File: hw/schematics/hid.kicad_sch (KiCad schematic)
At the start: 114 parts, among them M1 SK8701-01-004-MODULE, M2 SK8701-01-004-SENSOR, SW1 SW_Push, SW10 SW_Push, SW11 SW_Push, SW12 SW_Push, SW13 SW_Push, SW14 SW_Push, SW15 SW_Push, SW16 SW_Push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

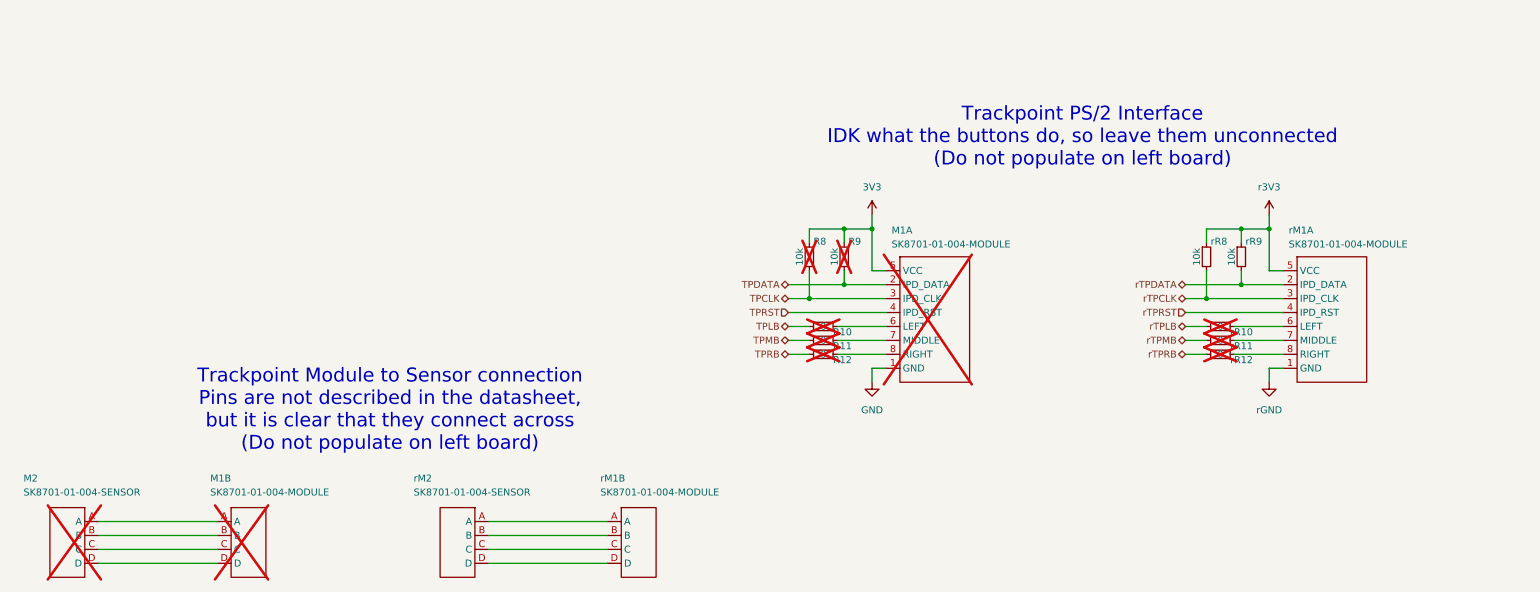
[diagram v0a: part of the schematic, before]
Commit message: Remove FPGA, no longer needed
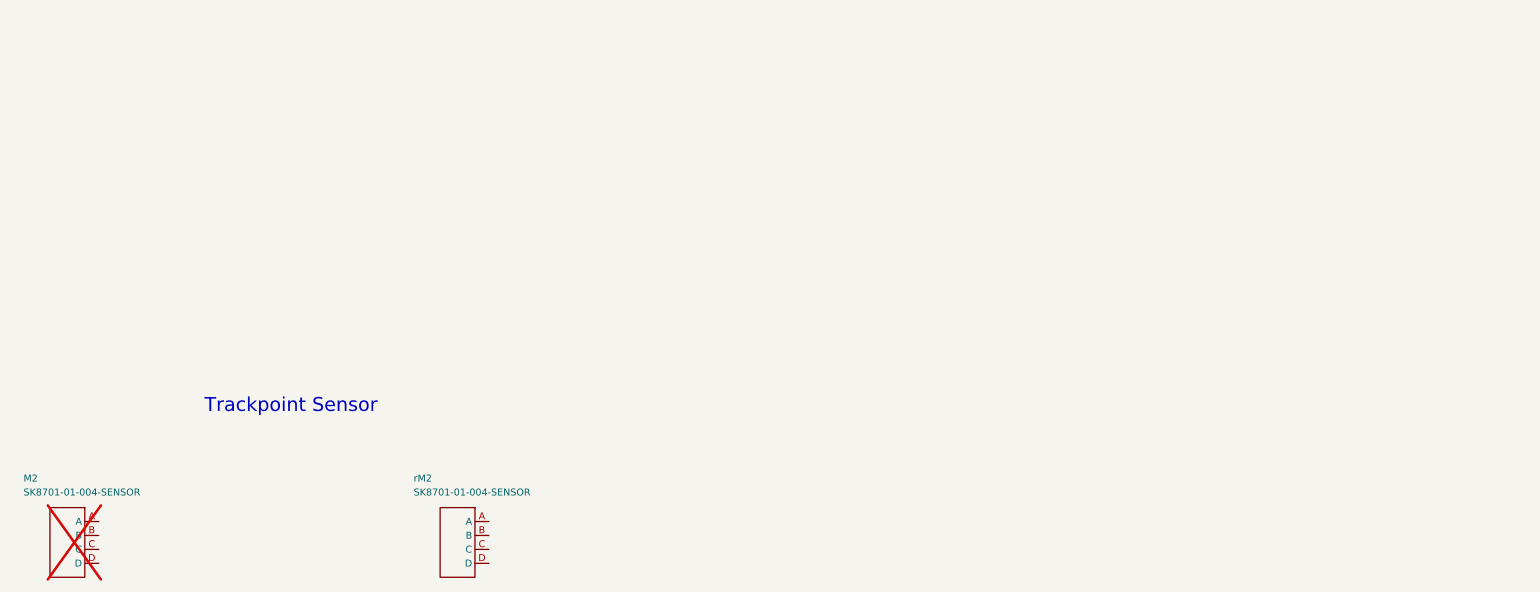
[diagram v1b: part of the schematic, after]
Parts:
- removed M1, rM1: SK8701-01-004-MODULE, symbol Alidade:SK8701-01-004-MODULE
- removed R10, R11, R12, rR10, rR11, rR12: 0, Alidade:0603, symbol Alidade:R
- removed R8, R9, rR8, rR9: 10k, Alidade:0603, symbol Alidade:R
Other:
- note added: "Trackpoint Sensor"
- note removed: "Trackpoint Module to Sensor connection Pins are not described in the datasheet, but it is clear that they connect across (Do not populate on left board)"
- note removed: "Trackpoint PS/2 Interface IDK what the buttons do, so leave them unconnected (Do not populate on left board)"

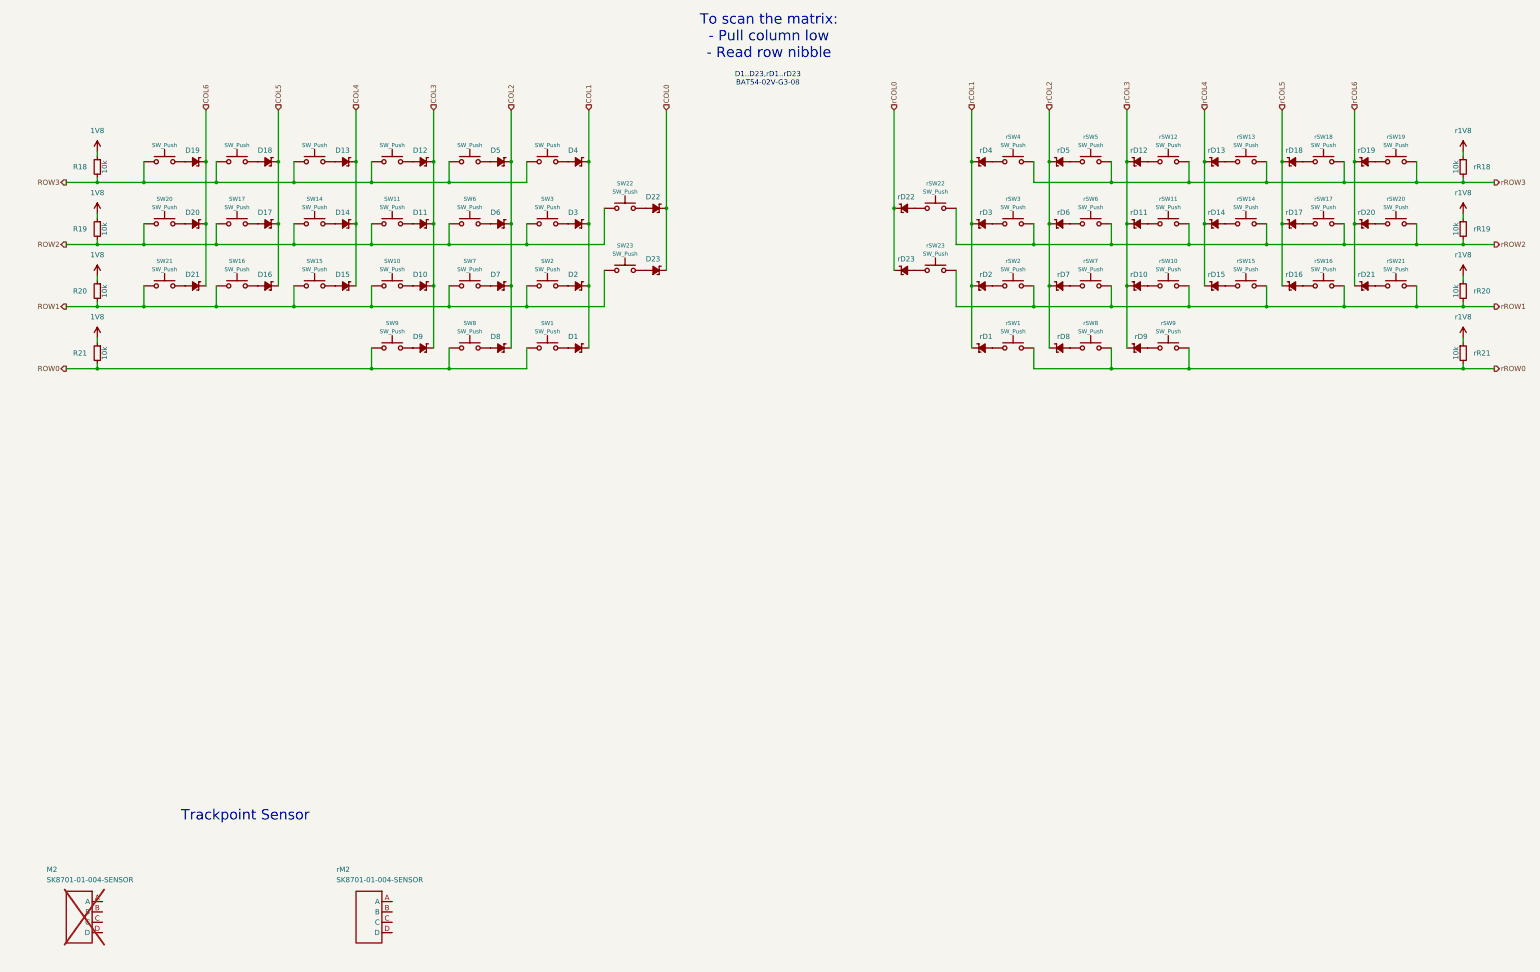
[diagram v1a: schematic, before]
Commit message: Update symbol, use ads122S for bridge measurement
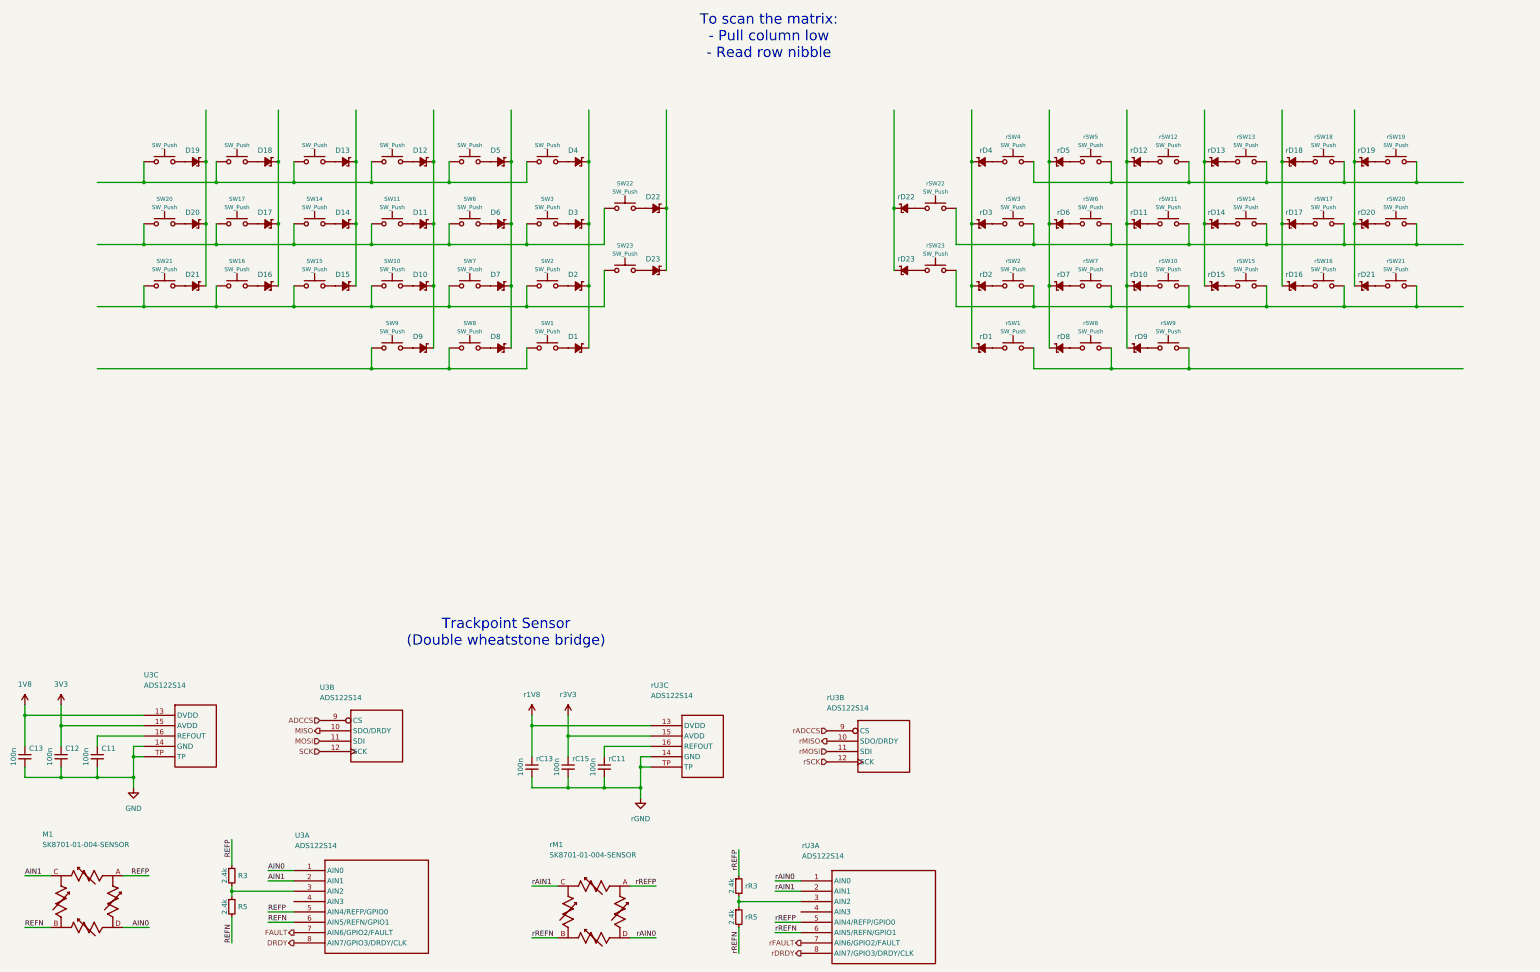
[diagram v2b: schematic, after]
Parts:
- removed R18, R19, R20, R21, rR18, rR19, rR20, rR21: 10k, Alidade:0603, symbol Alidade:R
- removed rM2: SK8701-01-004-SENSOR, Alidade:SK8707-01-SENSOR, symbol Alidade:SK8701-01-004-SENSOR
- added C11, C12, C13, rC11, rC13, rC15: 100n, symbol Alidade:C
- added R3, R5, rR3, rR5: 2.4k, symbol Alidade:R
- added U3, rU3: ADS122S14, symbol Alidade:ADS122S14
- added rM1: SK8701-01-004-SENSOR, Alidade:SK8707-01-SENSOR, symbol Alidade:SK8701-01-004-SENSOR
- M1: renamed from M2; now fitted
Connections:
- net 1V8: now also C13.1, U3.13 (DVDD)
- net r1V8: now also rC13.1, rU3.13 (DVDD)
- net REFP: now reaches M1.A
- net REFP: now also R3.1, U3.5 (AIN4/REFP/GPIO0)
- net REFN: now reaches M1.B
- net REFN: now also R5.2, U3.6 (AIN5/REFN/GPIO1)
- net AIN1: now reaches M1.C
- net AIN1: now also U3.2 (AIN1)
- net AIN0: now reaches M1.D
- net AIN0: now also U3.1 (AIN0)
- net COL0: no longer names the net of D22.3 (K), D23.3 (K)
- net COL1: no longer names the net of D1.3 (K), D2.3 (K), D3.3 (K), D4.3 (K)
- net COL2: no longer names the net of D5.3 (K), D6.3 (K), D7.3 (K), D8.3 (K)
- net COL3: no longer names the net of D10.3 (K), D11.3 (K), D12.3 (K), D9.3 (K)
- net COL4: no longer names the net of D13.3 (K), D14.3 (K), D15.3 (K)
- net COL5: no longer names the net of D16.3 (K), D17.3 (K), D18.3 (K)
- net COL6: no longer names the net of D19.3 (K), D20.3 (K), D21.3 (K)
- net ROW0: no longer names the net of SW1.1, SW8.1, SW9.1
- net ROW1: no longer names the net of SW10.1, SW15.1, SW16.1, SW2.1, SW21.1, SW23.2, SW7.1
- net ROW2: no longer names the net of SW11.1, SW14.1, SW17.1, SW20.1, SW22.2, SW3.1, SW6.1
- net ROW3: no longer names the net of SW12.1, SW13.1, SW18.1, SW19.1, SW4.1, SW5.1
- net rCOL0: no longer names the net of rD22.3 (K), rD23.3 (K)
- net rCOL1: no longer names the net of rD1.3 (K), rD2.3 (K), rD3.3 (K), rD4.3 (K)
- net rCOL2: no longer names the net of rD5.3 (K), rD6.3 (K), rD7.3 (K), rD8.3 (K)
- net rCOL3: no longer names the net of rD10.3 (K), rD11.3 (K), rD12.3 (K), rD9.3 (K)
- net rCOL4: no longer names the net of rD13.3 (K), rD14.3 (K), rD15.3 (K)
- net rCOL5: no longer names the net of rD16.3 (K), rD17.3 (K), rD18.3 (K)
- net rCOL6: no longer names the net of rD19.3 (K), rD20.3 (K), rD21.3 (K)
- net rROW0: no longer names the net of rSW1.1, rSW8.1, rSW9.1
- net rROW1: no longer names the net of rSW10.1, rSW15.1, rSW16.1, rSW2.1, rSW21.1, rSW23.2, rSW7.1
- net rROW2: no longer names the net of rSW11.1, rSW14.1, rSW17.1, rSW20.1, rSW22.2, rSW3.1, rSW6.1
- net rROW3: no longer names the net of rSW12.1, rSW13.1, rSW18.1, rSW19.1, rSW4.1, rSW5.1
- new net: R3.2, R5.1, U3.3 (AIN2)
- new net: rC11.1, rU3.16 (REFOUT)
- new net: C11.1, U3.16 (REFOUT)
- new net: rR3.2, rR5.1, rU3.3 (AIN2)
- new net 3V3: C12.1, U3.15 (AVDD)
- new net ADCCS: U3.9 (CS)
- new net DRDY: U3.8 (AIN7/GPIO3/DRDY/CLK)
- new net FAULT: U3.7 (AIN6/GPIO2/FAULT)
- new net GND: C11.2, C12.2, C13.2, U3.14 (GND), U3.TP
- new net MISO: U3.10 (SDO/DRDY)
- new net MOSI: U3.11 (SDI)
- new net SCK: U3.12 (SCK)
- new net r3V3: rC15.1, rU3.15 (AVDD)
- new net rADCCS: rU3.9 (CS)
- new net rAIN0: rM1.D, rU3.1 (AIN0)
- new net rAIN1: rM1.C, rU3.2 (AIN1)
- new net rDRDY: rU3.8 (AIN7/GPIO3/DRDY/CLK)
- new net rFAULT: rU3.7 (AIN6/GPIO2/FAULT)
- new net rGND: rC11.2, rC13.2, rC15.2, rU3.14 (GND), rU3.TP
- new net rMISO: rU3.10 (SDO/DRDY)
- new net rMOSI: rU3.11 (SDI)
- new net rREFN: rM1.B, rR5.2, rU3.6 (AIN5/REFN/GPIO1)
- new net rREFP: rM1.A, rR3.1, rU3.5 (AIN4/REFP/GPIO0)
- new net rSCK: rU3.12 (SCK)
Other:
- note added: "Trackpoint Sensor (Double wheatstone bridge)"
- note removed: "D1..D23,rD1..rD23 BAT54-02V-G3-08"
- note removed: "Trackpoint Sensor"

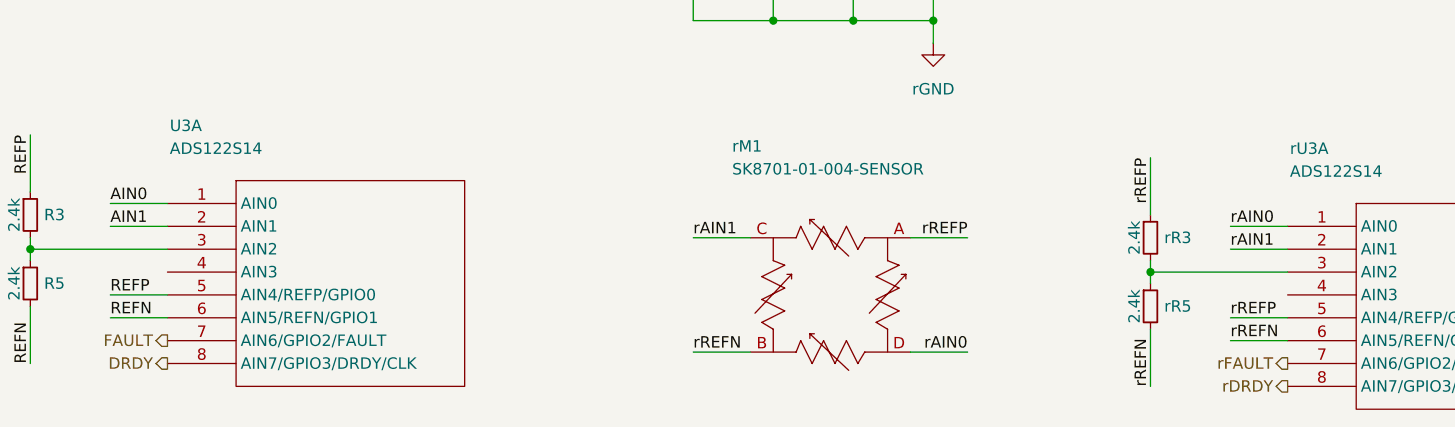
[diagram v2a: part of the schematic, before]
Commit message: Solve erc errors
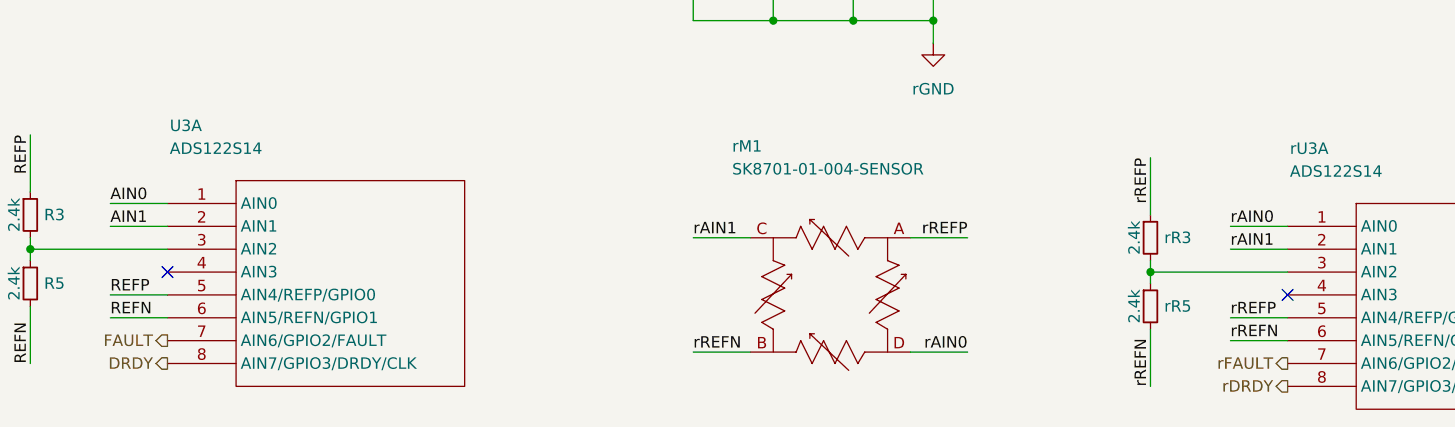
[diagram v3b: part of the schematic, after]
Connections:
- no-connect marks 0 -> 2
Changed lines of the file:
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@@
 		(color 0 0 0 0)
+	)
+	(no_connect
+		(at 91.44 252.73)
+	)
+	(no_connect
+		(at 215.9 255.27)
 	)
 	(wire
